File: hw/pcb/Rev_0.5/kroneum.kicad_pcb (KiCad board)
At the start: 2 copper layers, 40 x 40 mm, 23 parts, among them J1 USB_B_Micro, U1 STM32F042F4Px, U2 MCP1700-3302E_SOT89

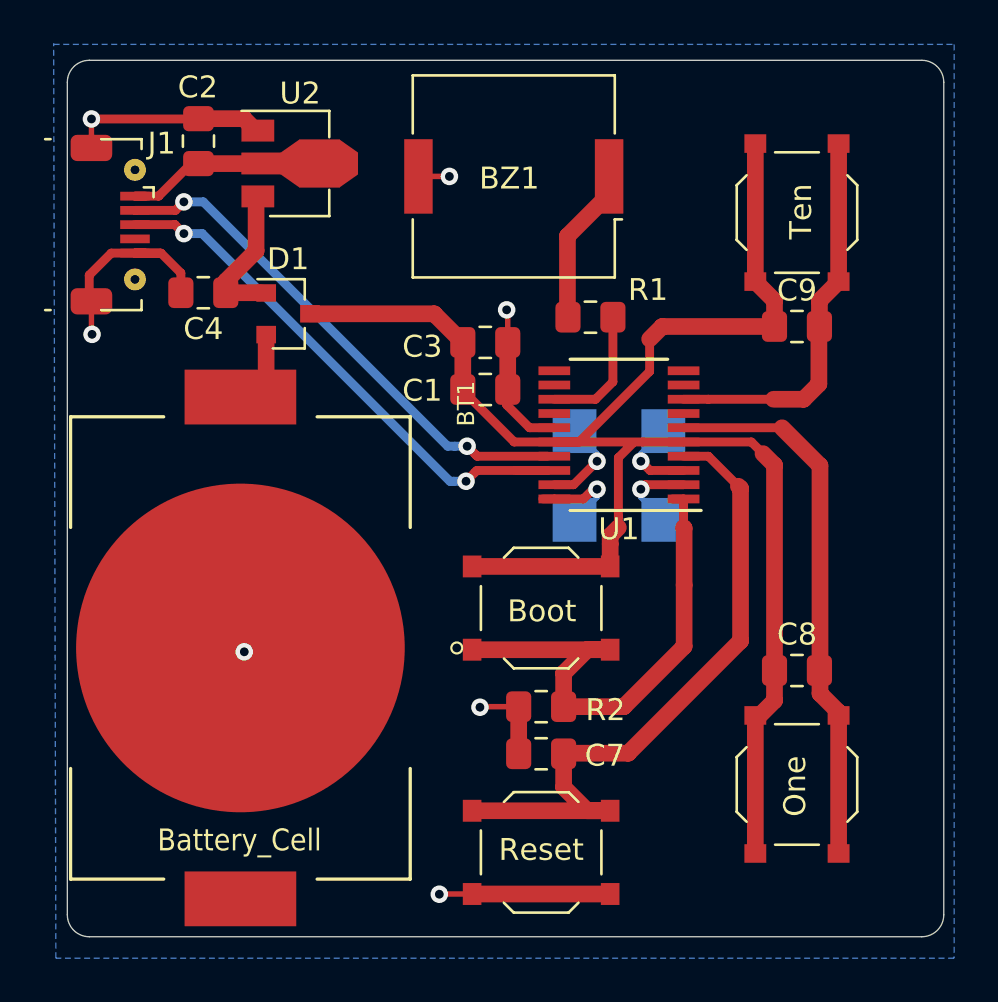
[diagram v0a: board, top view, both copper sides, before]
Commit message: [pcb] update SDW/SCL/SWCLK/SWDIO labels.
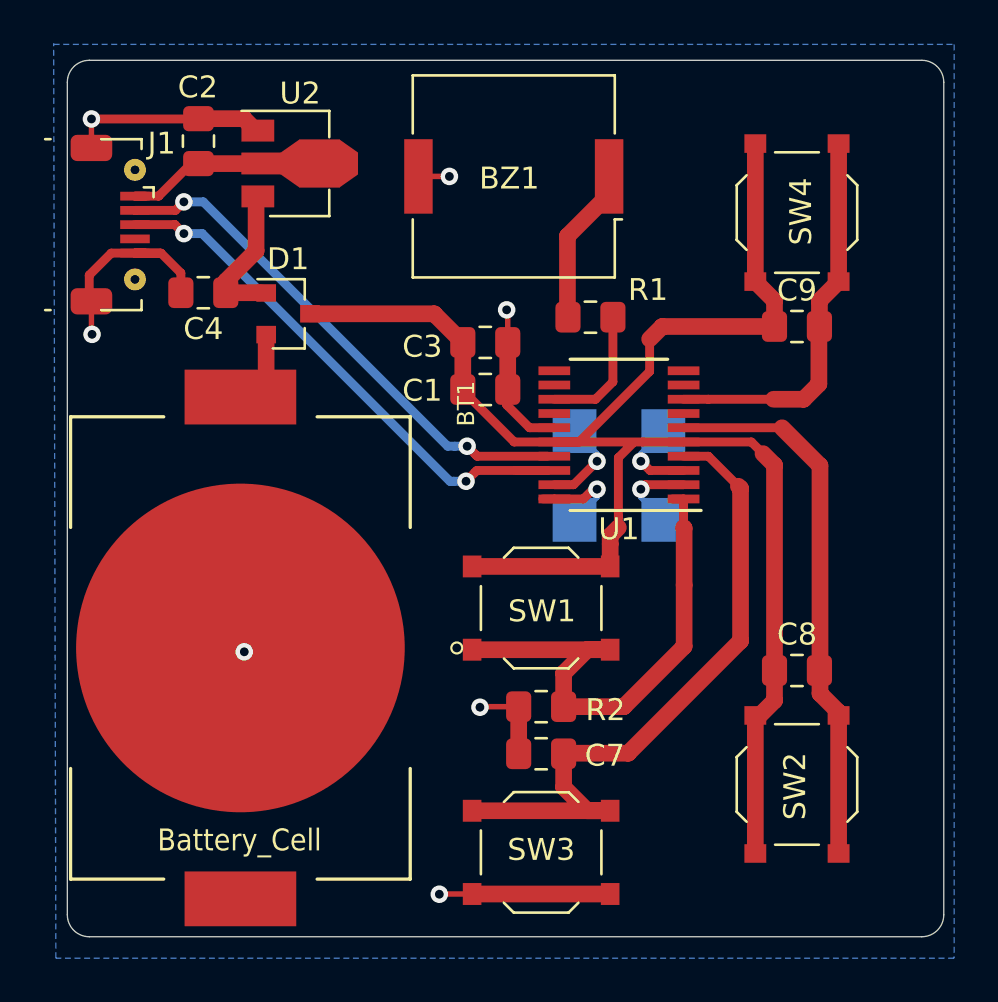
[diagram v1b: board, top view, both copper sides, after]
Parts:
- removed TP1, TP2: TestPoint, TestPoint:TestPoint_THTPad_2.0x2.0mm_Drill1.0mm
- added SCL: TestPoint, TestPoint:TestPoint_THTPad_2.0x2.0mm_Drill1.0mm, B.Cu at (153.6, 109.9)
- added SDA: TestPoint, TestPoint:TestPoint_THTPad_2.0x2.0mm_Drill1.0mm, B.Cu at (153.6, 113.9)
- SW1: renamed from Boot; value Boot -> Boot_Mode_Btn
- SW2: renamed from One; value One -> Ctrl_One_Btn
- SW3: renamed from Reset; value Reset -> Reset_Btn
- SW4: renamed from Ten; value Ten -> Ctrl_Ten_Btn
- renumbered TP3 to SWCLK, TP4 to SWDIO
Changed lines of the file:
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@@
     (31 B.Cu signal)
     (32 B.Adhes user hide)
-    (33 F.Adhes user hide)
+    (33 F.Adhes user)
     (34 B.Paste user hide)
-    (35 F.Paste user hide)
-    (36 B.SilkS user hide)
-    (37 F.SilkS user)
-    (38 B.Mask user hide)
-    (39 F.Mask user hide)
-    (40 Dwgs.User user hide)
-    (41 Cmts.User user hide)
+    (35 F.Paste user)
+    (36 B.SilkS user)
+    (37 F.SilkS user hide)
+    (38 B.Mask user)
+    (39 F.Mask user)
+    (40 Dwgs.User user)
+    (41 Cmts.User user)
     (42 Eco1.User user hide)
     (43 Eco2.User user hide)
@@
     (aux_axis_origin 166.39 132.94)
     (grid_origin 166.39 132.94)
-    (visible_elements FFFFFF7F)
+    (visible_elements FFFFFFFF)
     (pcbplotparams
       (layerselection 0x010fc_ffffffff)
@@
     (tags "test point THT pad rectangle square")
     (attr virtual)
-    (fp_text reference TP4 (at 0 1.998) (layer B.SilkS)
+    (fp_text reference SWDIO (at 0.75 2.375) (layer B.SilkS)
       (effects (font (size 1 1) (thickness 0.15)) (justify mirror))
     )
@@
     (tags "test point THT pad rectangle square")
     (attr virtual)
-    (fp_text reference TP3 (at 0.0002 -2.1748) (layer B.SilkS)
+    (fp_text reference SWCLK (at 0.95 -2.575) (layer B.SilkS)
       (effects (font (size 1 1) (thickness 0.15)) (justify mirror))
     )
@@
     (tags "test point THT pad rectangle square")
     (attr virtual)
-    (fp_text reference TP2 (at 0 1.998) (layer B.SilkS)
+    (fp_text reference SCL (at 0.04 2.375) (layer B.SilkS)
       (effects (font (size 1 1) (thickness 0.15)) (justify mirror))
     )
@@
     (tags "test point THT pad rectangle square")
     (attr virtual)
-    (fp_text reference TP1 (at 0 -2.1748) (layer B.SilkS)
+    (fp_text reference SDA (at 0.04 -2.575) (layer B.SilkS)
       (effects (font (size 1 1) (thickness 0.15)) (justify mirror))
     )
@@
     (tags "SPST Tactile Switch")
     (attr smd)
-    (fp_text reference One (at 0.08 0.09 270) (layer F.SilkS)
-      (effects (font (size 1 1) (thickness 0.15)))
-    )
-    (fp_text value One (at -0.05 0.025) (layer F.Fab)
+    (fp_text reference SW2 (at 0.08 0.09 270) (layer F.SilkS)
+      (effects (font (size 1 1) (thickness 0.15)))
+    )
+    (fp_text value Ctrl_One_Btn (at -0.05 0.025) (layer F.Fab)
       (effects (font (size 1 1) (thickness 0.15)))
     )
@@
     (tags "SPST Tactile Switch")
     (attr smd)
-    (fp_text reference Reset (at 0.005 -0.12) (layer F.SilkS)
-      (effects (font (size 1 1) (thickness 0.15)))
-    )
-    (fp_text value Reset (at -0.025 0) (layer F.Fab)
+    (fp_text reference SW3 (at 0.005 -0.12) (layer F.SilkS)
+      (effects (font (size 1 1) (thickness 0.15)))
+    )
+    (fp_text value Reset_Btn (at -0.025 0) (layer F.Fab)
       (effects (font (size 1 1) (thickness 0.15)))
     )
@@
     (tags "SPST Tactile Switch")
     (attr smd)
-    (fp_text reference Ten (at -0.05 -0.18 90) (layer F.SilkS)
-      (effects (font (size 1 1) (thickness 0.15)))
-    )
-    (fp_text value Ten (at 0.075 -0.025 180) (layer F.Fab)
+    (fp_text reference SW4 (at -0.05 -0.18 90) (layer F.SilkS)
+      (effects (font (size 1 1) (thickness 0.15)))
+    )
+    (fp_text value Ctrl_Ten_Btn (at 0.075 -0.025 180) (layer F.Fab)
       (effects (font (size 1 1) (thickness 0.15)))
     )
@@
     (tags "SPST Tactile Switch")
     (attr smd)
-    (fp_text reference Boot (at -0.035 -0.14 180) (layer F.SilkS)
-      (effects (font (size 1 1) (thickness 0.15)))
-    )
-    (fp_text value Boot (at 0.1 0.05) (layer F.Fab)
+    (fp_text reference SW1 (at -0.035 -0.14 180) (layer F.SilkS)
+      (effects (font (size 1 1) (thickness 0.15)))
+    )
+    (fp_text value Boot_Mode_Btn (at 0.1 0.05) (layer F.Fab)
       (effects (font (size 1 1) (thickness 0.15)))
     )
@@
     (pad 1 smd rect (at -11.45 0 270) (size 2.5 5.1) (layers F.Cu F.Paste F.Mask)
       (net 15 "Net-(BT1-Pad1)"))
-    (pad 1 smd rect (at 11.45 0 270) (size 2.5 5.1) (layers F.Cu F.Paste F.Mask))
+    (pad 1 smd rect (at 11.45 0 270) (size 2.5 5.1) (layers F.Cu F.Paste F.Mask)
+      (net 15 "Net-(BT1-Pad1)"))
     (pad 2 smd custom (at 0 0 270) (size 15 15) (layers F.Cu F.Paste F.Mask)
       (net 1 GND) (zone_connect 0)
